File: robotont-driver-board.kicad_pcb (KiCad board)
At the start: 2 copper layers, 40 x 55.1 mm, 31 parts, among them J1 PWR_IN, J2 ENC, J3 MOTOR, J4 Conn_02x05_Odd_Even, U1 NTMS4807N, U2 Si8641BD-B-IS, U3 MIC5205-X.X

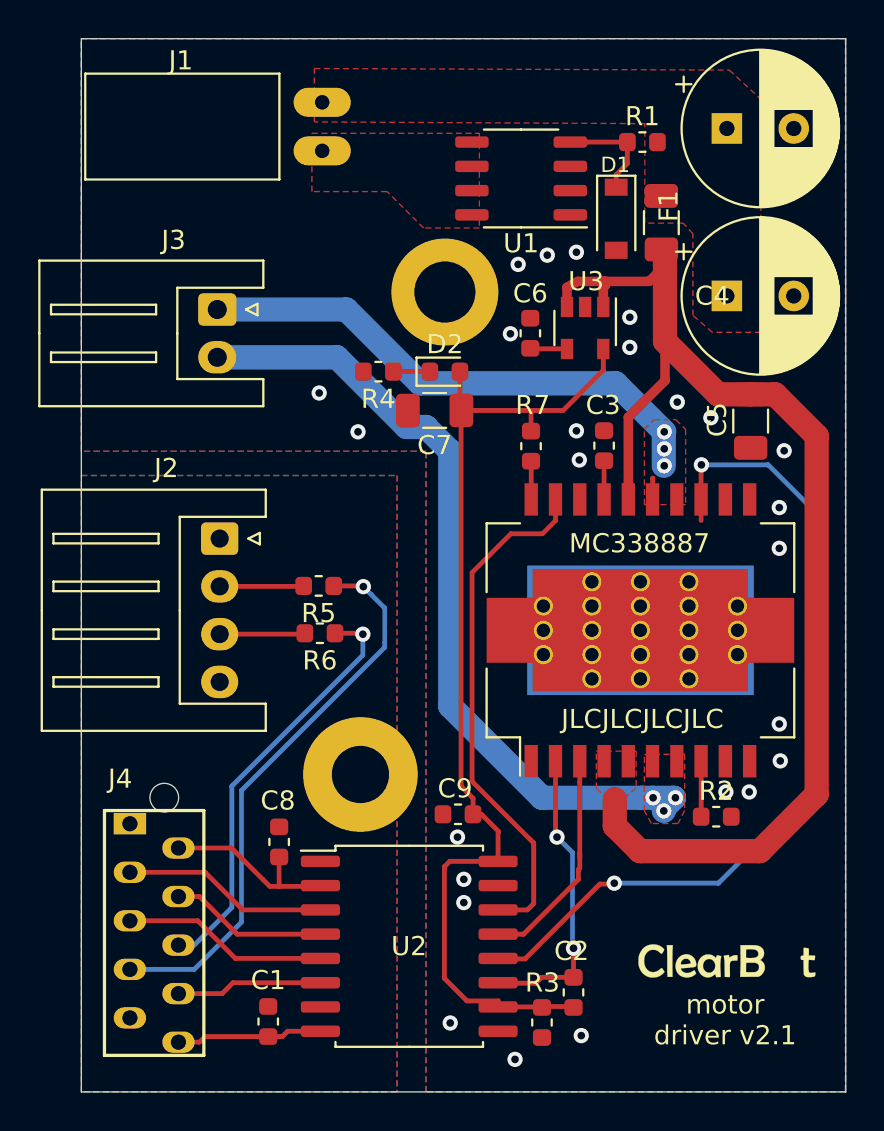
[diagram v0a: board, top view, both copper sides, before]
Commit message: some cleanup, CERN permissive license, included jlcpcb position files
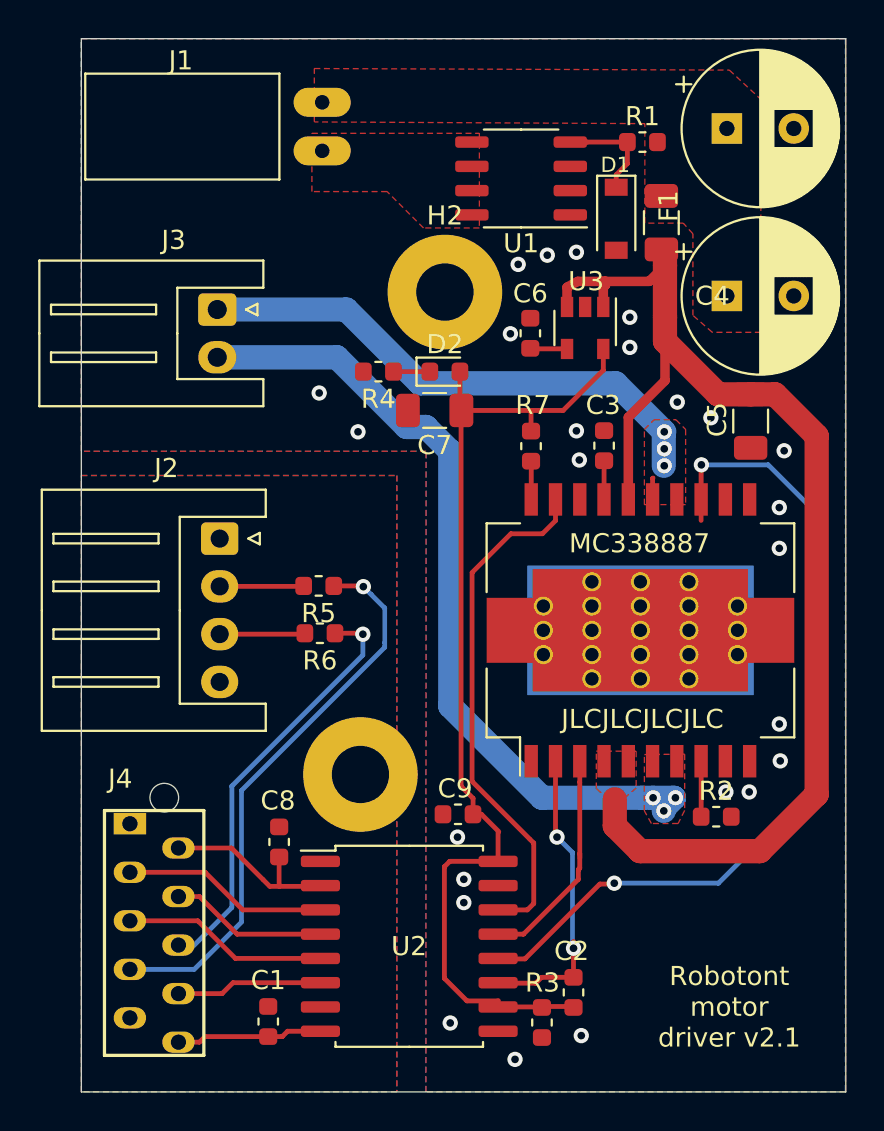
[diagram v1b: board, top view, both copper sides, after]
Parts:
- removed G***: LOGO, robotont-motor-board:clearbot_logo
- H2: footprint MountingHole:MountingHole_3.2mm_M3_DIN965_Pad -> MountingHole:MountingHole_3mm_Pad
- J1: footprint robotont-motor-board:KF2510-2AWG -> robotont-driver-board:KF2510-2AWG
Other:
- net class MotorClass added: clearance 0.4, trace_width 1.5, via_dia 0.8, via_drill 0.4
- net class motor removed
- board text added: "Robotont motor driver v2.1"
- board text removed: "motor driver v2.1"

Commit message: added production files
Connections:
- H1 pad 1: (no net) -> Net-(H1-Pad1)
- H2 pad 1: (no net) -> Net-(H2-Pad1)
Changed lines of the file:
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@@
-(kicad_pcb (version 20171130) (host pcbnew 5.1.7-a382d34a8~88~ubuntu18.04.1)
+(kicad_pcb (version 20171130) (host pcbnew 5.1.5+dfsg1-2build2)
   (general
     (thickness 1.6)
@@
     (zones 0)
     (modules 30)
-    (nets 28)
+    (nets 30)
   )
   (page A4)
   (layers
-    (0 F.Cu signal hide)
+    (0 F.Cu signal)
     (31 B.Cu signal hide)
     (32 B.Adhes user hide)
@@
   (net 26 /FAULT_D)
   (net 27 /FB_D)
+  (net 28 "Net-(H1-Pad1)")
+  (net 29 "Net-(H2-Pad1)")
   (net_class Default "This is the default net class."
     (clearance 0.2)
@@
     (add_net "Net-(D1-Pad1)")
     (add_net "Net-(D2-Pad1)")
+    (add_net "Net-(H1-Pad1)")
+    (add_net "Net-(H2-Pad1)")
     (add_net "Net-(J2-Pad2)")
     (add_net "Net-(J2-Pad3)")
@@
       (effects (font (size 1 1) (thickness 0.15)))
     )
-    (pad 1 thru_hole circle (at 0 0) (size 6 6) (drill 3) (layers *.Cu *.Mask))
+    (pad 1 thru_hole circle (at 0 0) (size 6 6) (drill 3) (layers *.Cu *.Mask)
+      (net 29 "Net-(H2-Pad1)"))
   )
   (module MountingHole:MountingHole_3mm_Pad (layer F.Cu)
@@
       (effects (font (size 1 1) (thickness 0.15)))
     )
-    (pad 1 thru_hole circle (at 0 0) (size 6 6) (drill 3) (layers *.Cu *.Mask))
+    (pad 1 thru_hole circle (at 0 0) (size 6 6) (drill 3) (layers *.Cu *.Mask)
+      (net 28 "Net-(H1-Pad1)"))
   )
   (module Package_SO:SO-8_3.9x4.9mm_P1.27mm (layer F.Cu)
